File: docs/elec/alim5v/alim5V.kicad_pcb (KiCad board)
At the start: 2 copper layers, 65 x 110.5 mm, 7 parts, among them P1 GND Ardui, P2 5V out, P3 MD49, P4 Charg, P5 Batt, SW1 SW, U1 UEI30-050-Q12P-C

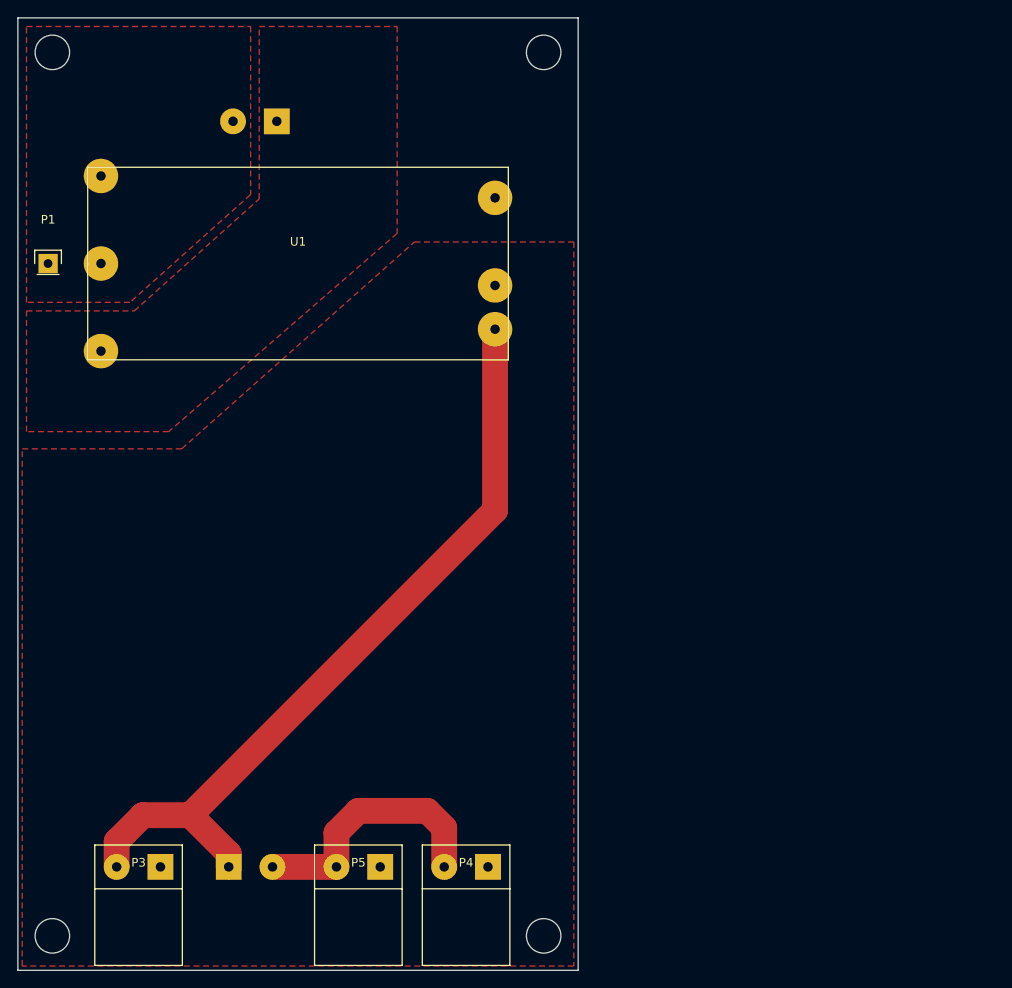
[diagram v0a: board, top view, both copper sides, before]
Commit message: ajout connecteur carte puissance
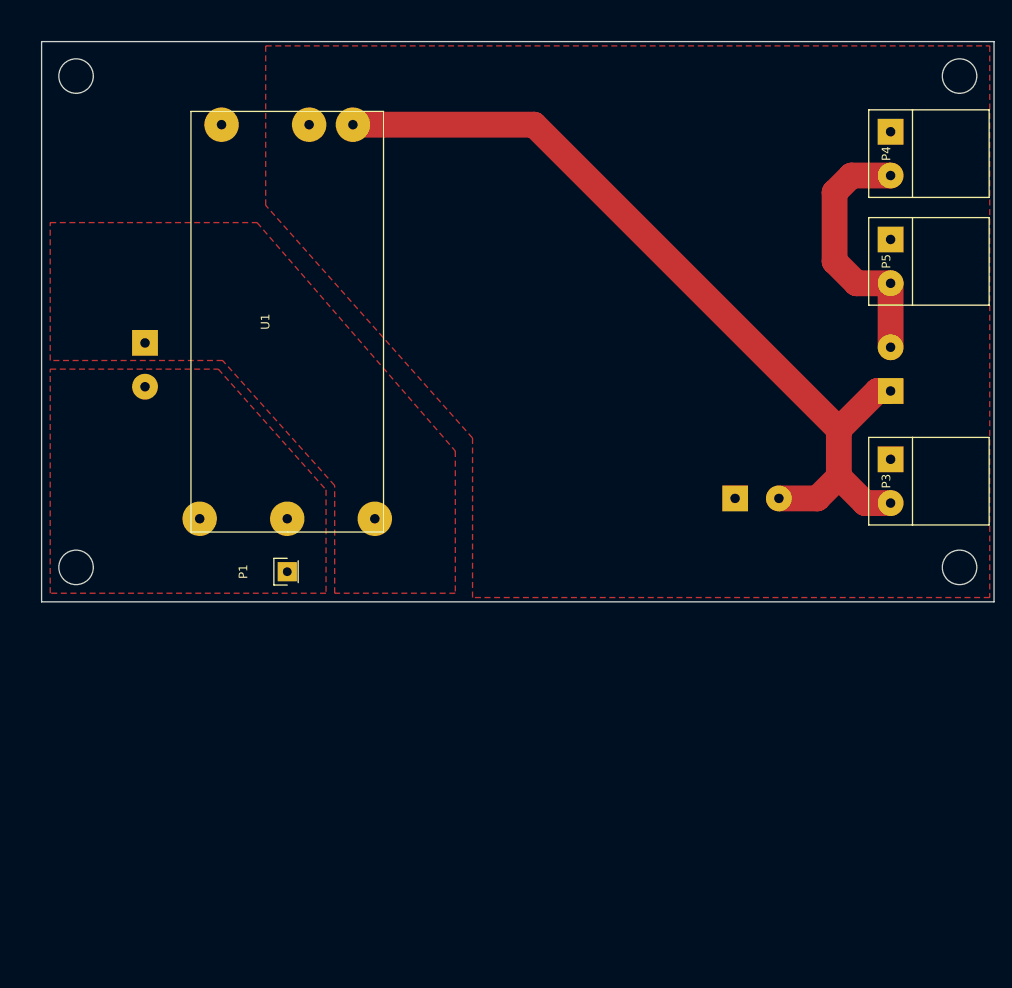
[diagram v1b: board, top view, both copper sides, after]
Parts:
- added P7: AUX, robair:Bornier5mm, B.Cu at (98.8, 68.8)
- moved P3 98.1 mm to (114.2, 66.8), turned to 270 degrees
- moved P4 96.3 mm to (114.2, 28.8), turned to 270 degrees
- moved SW1 94.1 mm to (114.2, 53.8), turned to 90 degrees
- moved P5 93.5 mm to (114.2, 41.2), turned to 270 degrees
- moved P1 45.3 mm to (44.2, 77.2), turned to 90 degrees
- moved P2 31.0 mm to (27.8, 53.2), turned to 270 degrees
- moved U1 6.86 mm to (44.2, 48.2), turned to 90 degrees
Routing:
- net Net-(P3-Pad2): track 91.6 -> 99.6 mm
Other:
- board size 65 x 110.5 mm -> 110.5 x 65 mm

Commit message: update elec
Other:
- outline, holes or cut-outs redrawn
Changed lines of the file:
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@@
     (last_trace_width 3)
     (trace_clearance 0.8)
-    (zone_clearance 0.8)
+    (zone_clearance 2)
     (zone_45_only no)
     (trace_min 0.2)
@@
       (net 4 "Net-(P3-Pad2)"))
   )
-  (gr_circle (center 19.75 76.75) (end 19.75 74.75) (layer Edge.Cuts) (width 0.15))
-  (gr_circle (center 19.75 19.75) (end 19.75 21.75) (layer Edge.Cuts) (width 0.15))
-  (gr_circle (center 122.25 76.75) (end 122.25 74.75) (layer Edge.Cuts) (width 0.15))
-  (gr_circle (center 122.25 19.75) (end 122.25 17.75) (layer Edge.Cuts) (width 0.15))
+  (gr_circle (center 20.25 76.75) (end 20.25 74.75) (layer Edge.Cuts) (width 0.15))
+  (gr_circle (center 20.25 19.75) (end 20.25 21.75) (layer Edge.Cuts) (width 0.15))
+  (gr_circle (center 118.25 76.75) (end 118.25 74.75) (layer Edge.Cuts) (width 0.15))
+  (gr_circle (center 118.25 19.75) (end 118.25 17.75) (layer Edge.Cuts) (width 0.15))
   (gr_line (start 15.75 15.75) (end 15.75 80.75) (angle 90) (layer Edge.Cuts) (width 0.15))
   (gr_line (start 126.25 15.75) (end 15.75 15.75) (angle 90) (layer Edge.Cuts) (width 0.15))
@@
   (segment (start 109.71 31.29) (end 107.75 33.25) (width 3) (layer F.Cu) (net 7))
   (zone (net 3) (net_name /GND24) (layer F.Cu) (hatch edge 0.508)
-    (connect_pads (clearance 0.8))
+    (connect_pads (clearance 2))
     (min_thickness 0.254)
     (fill yes (arc_segments 16) (thermal_gap 0.8) (thermal_bridge_width 0.8))
@@
   )
   (zone (net 2) (net_name "Net-(P2-Pad1)") (layer F.Cu) (hatch edge 0.508)
-    (connect_pads (clearance 0.8))
+    (connect_pads (clearance 2))
     (min_thickness 0.254)
     (fill yes (arc_segments 16) (thermal_gap 0.8) (thermal_bridge_width 0.8))
@@
   )
   (zone (net 1) (net_name /GND5) (layer F.Cu) (hatch edge 0.508)
-    (connect_pads (clearance 0.8))
+    (connect_pads (clearance 2))
     (min_thickness 0.254)
     (fill yes (arc_segments 16) (thermal_gap 0.8) (thermal_bridge_width 0.8))
